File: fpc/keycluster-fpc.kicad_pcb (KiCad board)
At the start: 2 copper layers, 4 x 21.3 mm, 4 parts

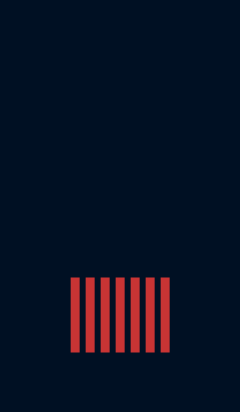
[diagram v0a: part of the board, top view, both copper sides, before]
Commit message: Delete redundant pads.
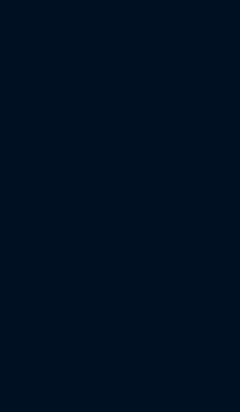
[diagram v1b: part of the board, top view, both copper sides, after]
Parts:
- removed the REF** at (213.0, 1010.0)
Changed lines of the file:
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@@
     (tracks 58)
     (zones 0)
-    (modules 4)
+    (modules 3)
     (nets 1)
   )
@@
     (pad 1 smd rect (at -1.5 0) (size 0.3 2.5) (layers B.Cu B.Mask))
   )
-  (module UGL:Keycluster_FPC_7x0.5_pads (layer F.Cu)
-    (at 213 1010)
-    (attr smd)
-    (fp_text reference REF** (at 0 3.65) (layer F.SilkS) hide
-      (effects (font (size 1 1) (thickness 0.15)))
-    )
-    (fp_text value Keycluster_FPC_7x0.5_pads (at 0 4.8) (layer F.Fab)
-      (effects (font (size 1 1) (thickness 0.15)))
-    )
-    (pad 7 smd rect (at 1.5 0) (size 0.3 2.5) (layers F.Cu F.Mask))
-    (pad 6 smd rect (at 1 0) (size 0.3 2.5) (layers F.Cu F.Mask))
-    (pad 5 smd rect (at 0.5 0) (size 0.3 2.5) (layers F.Cu F.Mask))
-    (pad 4 smd rect (at 0 0) (size 0.3 2.5) (layers F.Cu F.Mask))
-    (pad 3 smd rect (at -0.5 0) (size 0.3 2.5) (layers F.Cu F.Mask))
-    (pad 2 smd rect (at -1 0) (size 0.3 2.5) (layers F.Cu F.Mask))
-    (pad 1 smd rect (at -1.5 0) (size 0.3 2.5) (layers F.Cu F.Mask))
-  )
   (gr_text "keycluster_fpc\n2.0.0" (at 213 119.3 90) (layer B.SilkS)
